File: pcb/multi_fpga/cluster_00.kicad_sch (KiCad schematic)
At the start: 7 parts, among them J1 Cluster0_SpokeBus, J2 Cluster0_Power

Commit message: Fixed C footprint.
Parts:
- C2, C3: footprint Capacitor_SMD:C_0201_0603Metric -> Capacitor_SMD:C_0603_1608Metric
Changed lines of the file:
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@@
 			)
 		)
-		(property "Footprint" "Capacitor_SMD:C_0201_0603Metric"
+		(property "Footprint" "Capacitor_SMD:C_0603_1608Metric"
 			(at 328.6252 198.12 0)
 			(hide yes)
@@
 			)
 		)
-		(property "Footprint" "Capacitor_SMD:C_0201_0603Metric"
+		(property "Footprint" "Capacitor_SMD:C_0603_1608Metric"
 			(at 290.5252 198.12 0)
 			(hide yes)
@@
 		)
 	)
+	(embedded_fonts no)
 )

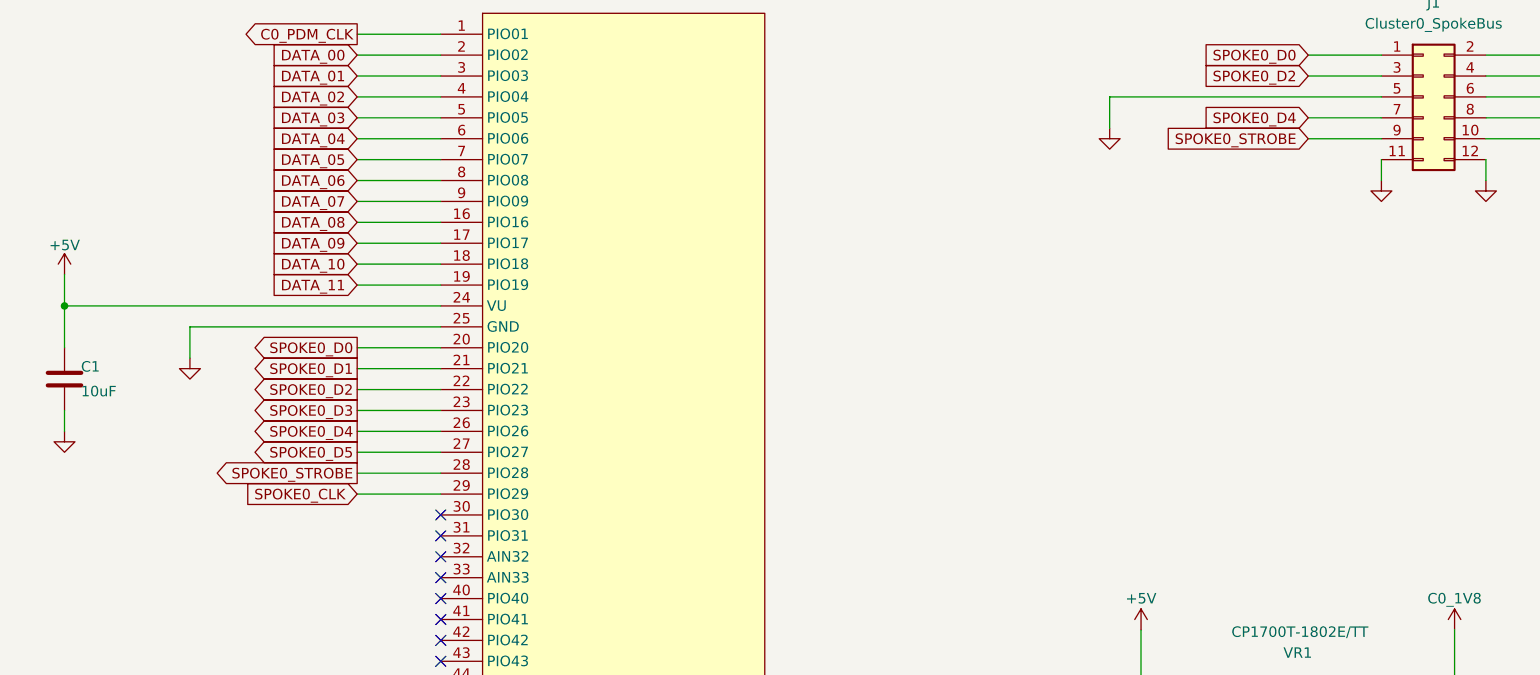
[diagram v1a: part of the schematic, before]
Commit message: Added FPGA_RESET_N signal.
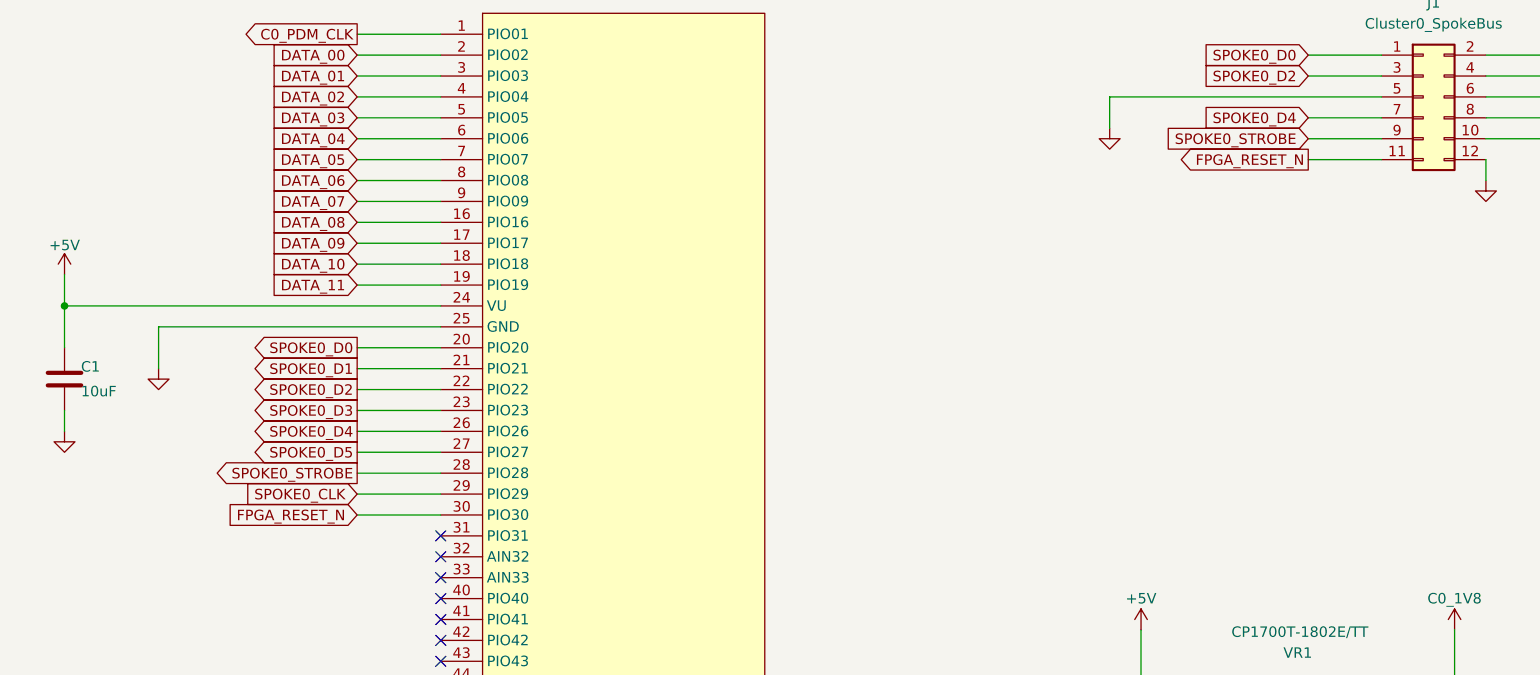
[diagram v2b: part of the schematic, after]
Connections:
- net GND: no longer J1.11 (Pin_11)
- net FPGA_RESET_N: now reaches A1.30 (PIO30)
- net FPGA_RESET_N: now also J1.11 (Pin_11)
- no-connect marks 13 -> 12
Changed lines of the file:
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@@
 	)
 	(no_connect
-		(at 204.47 167.64)
-	)
-	(no_connect
 		(at 204.47 175.26)
 	)
@@
 	(wire
 		(pts
-			(xy 173.99 144.78) (xy 204.47 144.78)
+			(xy 170.18 144.78) (xy 204.47 144.78)
 		)
 		(stroke
@@
 	(wire
 		(pts
+			(xy 204.47 167.64) (xy 194.31 167.64)
+		)
+		(stroke
+			(width 0)
+			(type default)
+		)
+	)
+	(wire
+		(pts
 			(xy 309.88 114.3) (xy 318.77 114.3)
 		)
@@
 	(wire
 		(pts
-			(xy 173.99 148.59) (xy 173.99 144.78)
+			(xy 170.18 149.86) (xy 170.18 144.78)
 		)
 		(stroke
@@
 	(wire
 		(pts
+			(xy 309.88 124.46) (xy 318.77 124.46)
+		)
+		(stroke
+			(width 0)
+			(type default)
+		)
+	)
+	(wire
+		(pts
 			(xy 331.47 111.76) (xy 342.9 111.76)
 		)
@@
 	(wire
 		(pts
-			(xy 318.77 124.46) (xy 318.77 127)
-		)
-		(stroke
-			(width 0)
-			(type default)
-		)
-	)
-	(wire
-		(pts
 			(xy 204.47 137.16) (xy 194.31 137.16)
 		)
@@
 		)
 	)
+	(global_label "FPGA_RESET_N"
+		(shape output)
+		(at 309.88 124.46 180)
+		(effects
+			(font
+				(size 1.27 1.27)
+			)
+			(justify right)
+		)
+		(property "Intersheetrefs" "${INTERSHEET_REFS}"
+			(at 309.88 124.46 180)
+			(hide yes)
+			(show_name no)
+			(do_not_autoplace no)
+			(effects
+				(font
+					(size 1.27 1.27)
+				)
+			)
+		)
+	)
 	(global_label "SPOKE0_STROBE"
 		(shape input)
@@
 		)
 	)
+	(global_label "FPGA_RESET_N"
+		(shape input)
+		(at 194.31 167.64 180)
+		(effects
+			(font
+				(size 1.27 1.27)
+			)
+			(justify right)
+		)
+		(property "Intersheetrefs" "${INTERSHEET_REFS}"
+			(at 194.31 167.64 180)
+			(hide yes)
+			(show_name no)
+			(do_not_autoplace no)
+			(effects
+				(font
+					(size 1.27 1.27)
+				)
+			)
+		)
+	)
 	(global_label "DATA_05"
 		(shape input)
@@
 	(symbol
 		(lib_id "power:GND")
-		(at 173.99 148.59 0)
+		(at 170.18 149.86 0)
 		(unit 1)
 		(body_style 1)
@@
 		(dnp no)
 		(property "Reference" "#PWR03"
-			(at 173.99 148.59 0)
+			(at 170.18 149.86 0)
 			(hide yes)
 			(show_name no)
@@
 		)
 		(property "Value" "GND"
-			(at 173.99 148.59 0)
+			(at 170.18 149.86 0)
 			(hide yes)
 			(show_name no)
@@
 		)
 		(property "Footprint" ""
-			(at 173.99 148.59 0)
+			(at 170.18 149.86 0)
 			(hide yes)
 			(show_name no)
@@
 		)
 		(property "Datasheet" ""
-			(at 173.99 148.59 0)
+			(at 170.18 149.86 0)
 			(hide yes)
 			(show_name no)
@@
 		)
 		(property "Description" "Power symbol creates a global label with name \"GND\" , ground"
-			(at 173.99 148.59 0)
+			(at 170.18 149.86 0)
 			(hide yes)
 			(show_name no)
@@
 	)
 	(symbol
-		(lib_id "power:GND")
-		(at 318.77 127 0)
-		(unit 1)
-		(body_style 1)
-		(exclude_from_sim no)
-		(in_bom yes)
-		(on_board yes)
-		(in_pos_files yes)
-		(dnp no)
-		(property "Reference" "#PWR08"
-			(at 318.77 127 0)
-			(hide yes)
-			(show_name no)
-			(do_not_autoplace no)
-			(effects
-				(font
-					(size 1.27 1.27)
-				)
-			)
-		)
-		(property "Value" "GND"
-			(at 318.77 127 0)
-			(hide yes)
-			(show_name no)
-			(do_not_autoplace no)
-			(effects
-				(font
-					(size 1.27 1.27)
-				)
-			)
-		)
-		(property "Footprint" ""
-			(at 318.77 127 0)
-			(hide yes)
-			(show_name no)
-			(do_not_autoplace no)
-			(effects
-				(font
-					(size 1.27 1.27)
-				)
-			)
-		)
-		(property "Datasheet" ""
-			(at 318.77 127 0)
-			(hide yes)
-			(show_name no)
-			(do_not_autoplace no)
-			(effects
-				(font
-					(size 1.27 1.27)
-				)
-			)
-		)
-		(property "Description" "Power symbol creates a global label with name \"GND\" , ground"
-			(at 318.77 127 0)
-			(hide yes)
-			(show_name no)
-			(do_not_autoplace no)
-			(effects
-				(font
-					(size 1.27 1.27)
-				)
-			)
-		)
-		(pin "1"
-		)
-		(instances
-			(project "top"
-				(path "/80f109c4-96c5-4385-bfb6-0f7a96b014ab/a9226103-652b-4861-8232-5e03f261e340"
-					(reference "#PWR08")
-					(unit 1)
-				)
-			)
-			(project "cluster_00"
-				(path "/b195ece8-c162-43a0-9657-a279941605a3"
-					(reference "#PWR08")
-					(unit 1)
-				)
-			)
-		)
-	)
-	(symbol
 		(lib_id "Device:C")
 		(at 158.75 151.13 0)
@@
 		)
 	)
-	(embedded_fonts no)
 )

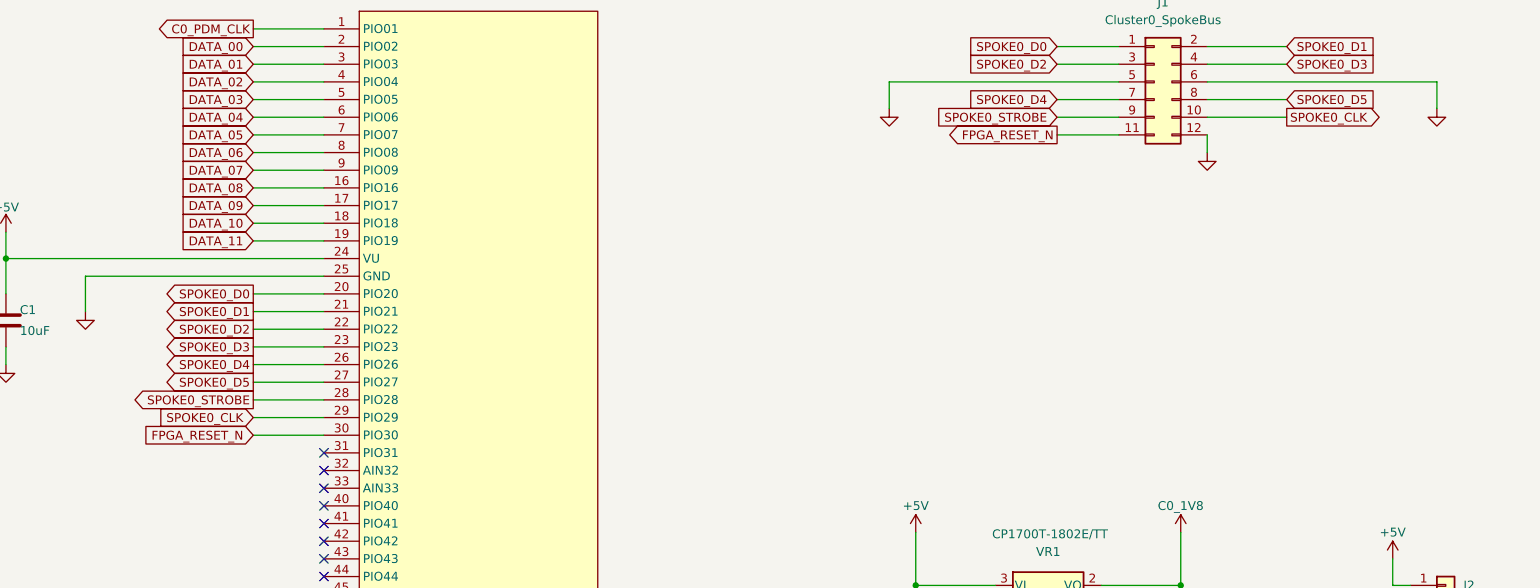
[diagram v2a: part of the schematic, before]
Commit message: Added spoke alive signals.
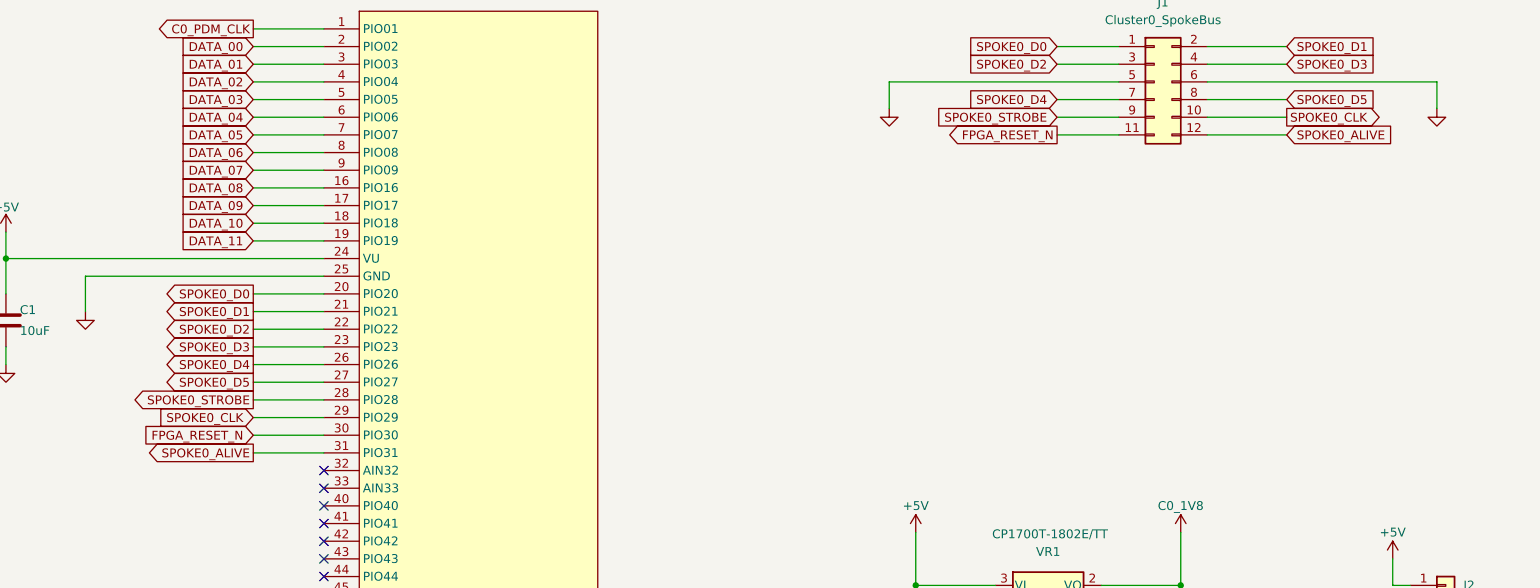
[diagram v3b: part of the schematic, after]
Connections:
- net GND: no longer J1.12 (Pin_12)
- net SPOKE0_ALIVE: now reaches A1.31 (PIO31)
- net SPOKE0_ALIVE: now also J1.12 (Pin_12)
- no-connect marks 12 -> 11
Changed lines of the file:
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@@
-	)
-	(no_connect
-		(at 204.47 170.18)
 	)
 	(no_connect
@@
 	(wire
 		(pts
+			(xy 331.47 124.46) (xy 342.9 124.46)
+		)
+		(stroke
+			(width 0)
+			(type default)
+		)
+	)
+	(wire
+		(pts
 			(xy 204.47 152.4) (xy 194.31 152.4)
 		)
@@
 	(wire
 		(pts
-			(xy 331.47 124.46) (xy 331.47 127)
-		)
-		(stroke
-			(width 0)
-			(type default)
-		)
-	)
-	(wire
-		(pts
 			(xy 327.66 181.61) (xy 327.66 189.23)
 		)
@@
 		(pts
 			(xy 327.66 189.23) (xy 316.23 189.23)
+		)
+		(stroke
+			(width 0)
+			(type default)
+		)
+	)
+	(wire
+		(pts
+			(xy 194.31 170.18) (xy 204.47 170.18)
 		)
 		(stroke
@@
 		)
 	)
+	(global_label "SPOKE0_ALIVE"
+		(shape input)
+		(at 342.9 124.46 0)
+		(fields_autoplaced yes)
+		(effects
+			(font
+				(size 1.27 1.27)
+			)
+			(justify left)
+		)
+		(property "Intersheetrefs" "${INTERSHEET_REFS}"
+			(at 359.2504 124.46 0)
+			(hide yes)
+			(show_name no)
+			(do_not_autoplace no)
+			(effects
+				(font
+					(size 1.27 1.27)
+				)
+				(justify left)
+			)
+		)
+	)
 	(global_label "FPGA_RESET_N"
 		(shape output)
@@
 					(size 1.27 1.27)
 				)
+			)
+		)
+	)
+	(global_label "SPOKE0_ALIVE"
+		(shape output)
+		(at 194.31 170.18 180)
+		(fields_autoplaced yes)
+		(effects
+			(font
+				(size 1.27 1.27)
+			)
+			(justify right)
+		)
+		(property "Intersheetrefs" "${INTERSHEET_REFS}"
+			(at 177.9596 170.18 0)
+			(hide yes)
+			(show_name no)
+			(do_not_autoplace no)
+			(effects
+				(font
+					(size 1.27 1.27)
+				)
+				(justify right)
 			)
 		)
@@
 					(unit 1)
 				)
-			)
-		)
-	)
-	(symbol
-		(lib_id "power:GND")
-		(at 331.47 127 0)
-		(unit 1)
-		(body_style 1)
-		(exclude_from_sim no)
-		(in_bom yes)
-		(on_board yes)
-		(in_pos_files yes)
-		(dnp no)
-		(property "Reference" "#PWR011"
-			(at 331.47 127 0)
-			(hide yes)
-			(show_name no)
-			(do_not_autoplace no)
-			(effects
-				(font
-					(size 1.27 1.27)
-				)
-			)
-		)
-		(property "Value" "GND"
-			(at 331.47 127 0)
-			(hide yes)
-			(show_name no)
-			(do_not_autoplace no)
-			(effects
-				(font
-					(size 1.27 1.27)
-				)
-			)
-		)
-		(property "Footprint" ""
-			(at 331.47 127 0)
-			(hide yes)
-			(show_name no)
-			(do_not_autoplace no)
-			(effects
-				(font
-					(size 1.27 1.27)
-				)
-			)
-		)
-		(property "Datasheet" ""
-			(at 331.47 127 0)
-			(hide yes)
-			(show_name no)
-			(do_not_autoplace no)
-			(effects
-				(font
-					(size 1.27 1.27)
-				)
-			)
-		)
-		(property "Description" "Power symbol creates a global label with name \"GND\" , ground"
-			(at 331.47 127 0)
-			(hide yes)
-			(show_name no)
-			(do_not_autoplace no)
-			(effects
-				(font
-					(size 1.27 1.27)
-				)
-			)
-		)
-		(pin "1"
-		)
-		(instances
-			(project "top"
-				(path "/80f109c4-96c5-4385-bfb6-0f7a96b014ab/a9226103-652b-4861-8232-5e03f261e340"
-					(reference "#PWR011")
-					(unit 1)
-				)
-			)
-			(project "cluster_00"
-				(path "/b195ece8-c162-43a0-9657-a279941605a3"
-					(reference "#PWR011")
-					(unit 1)
-				)

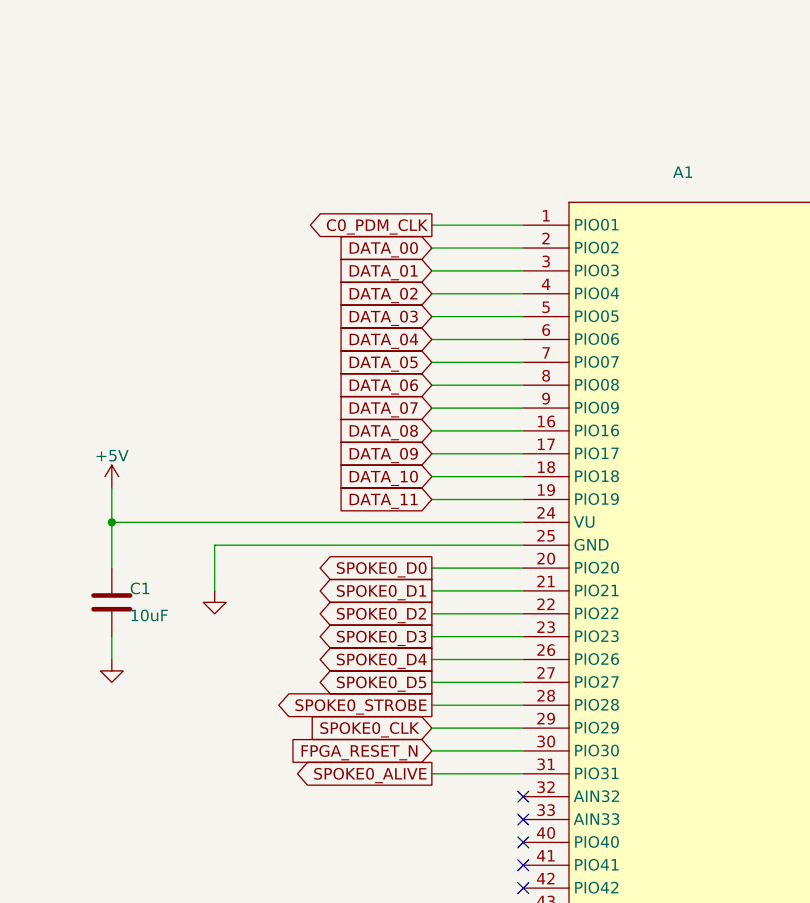
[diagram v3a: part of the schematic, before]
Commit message: Moved clock pin.
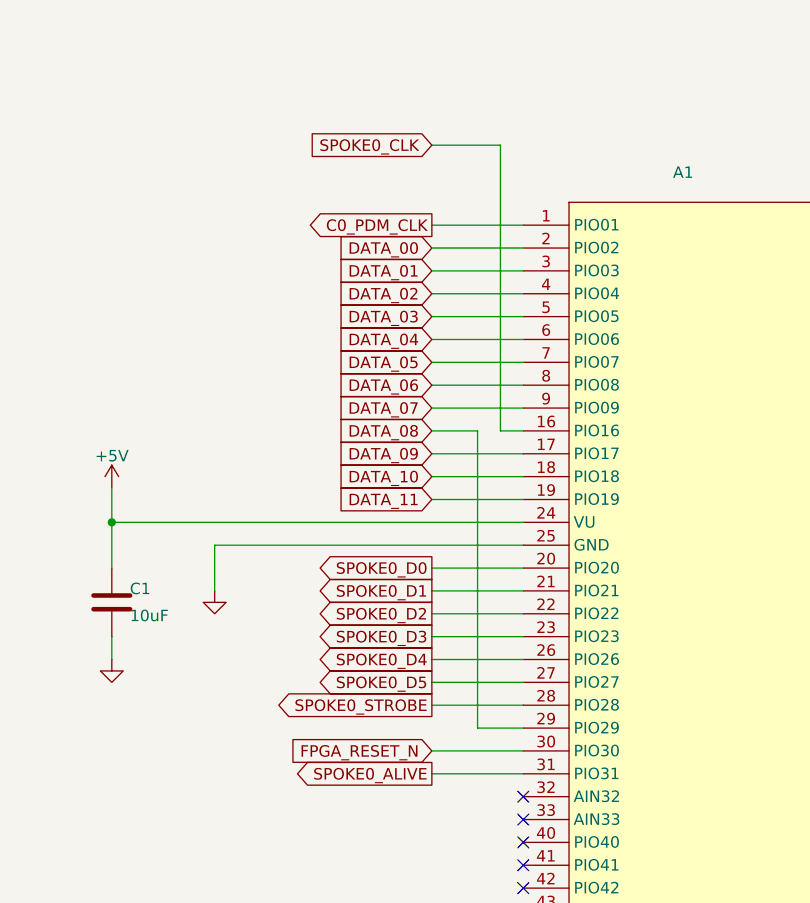
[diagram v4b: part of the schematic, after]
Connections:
- net DATA_08: now also A1.29 (PIO29); no longer A1.16 (PIO16)
- net SPOKE0_CLK: now also A1.16 (PIO16); no longer A1.29 (PIO29)
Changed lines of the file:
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@@
 	(wire
 		(pts
-			(xy 204.47 165.1) (xy 194.31 165.1)
+			(xy 204.47 165.1) (xy 199.39 165.1)
 		)
 		(stroke
@@
 	(wire
 		(pts
+			(xy 201.93 132.08) (xy 204.47 132.08)
+		)
+		(stroke
+			(width 0)
+			(type default)
+		)
+	)
+	(wire
+		(pts
 			(xy 204.47 162.56) (xy 194.31 162.56)
 		)
@@
 	(wire
 		(pts
+			(xy 194.31 132.08) (xy 199.39 132.08)
+		)
+		(stroke
+			(width 0)
+			(type default)
+		)
+	)
+	(wire
+		(pts
 			(xy 327.66 181.61) (xy 327.66 189.23)
 		)
@@
 	(wire
 		(pts
+			(xy 201.93 100.33) (xy 201.93 132.08)
+		)
+		(stroke
+			(width 0)
+			(type default)
+		)
+	)
+	(wire
+		(pts
 			(xy 358.14 185.42) (xy 358.14 189.23)
 		)
@@
 	(wire
 		(pts
+			(xy 194.31 100.33) (xy 201.93 100.33)
+		)
+		(stroke
+			(width 0)
+			(type default)
+		)
+	)
+	(wire
+		(pts
 			(xy 327.66 189.23) (xy 316.23 189.23)
 		)
@@
 	(wire
 		(pts
+			(xy 199.39 132.08) (xy 199.39 165.1)
+		)
+		(stroke
+			(width 0)
+			(type default)
+		)
+	)
+	(wire
+		(pts
 			(xy 358.14 195.58) (xy 358.14 191.77)
 		)
@@
 		(pts
 			(xy 309.88 119.38) (xy 318.77 119.38)
-		)
-		(stroke
-			(width 0)
-			(type default)
-		)
-	)
-	(wire
-		(pts
-			(xy 204.47 132.08) (xy 194.31 132.08)
 		)
 		(stroke
@@
 	(global_label "SPOKE0_CLK"
 		(shape input)
-		(at 194.31 165.1 180)
-		(effects
-			(font
-				(size 1.27 1.27)
-			)
-			(justify right)
-		)
-		(property "Intersheetrefs" "${INTERSHEET_REFS}"
-			(at 194.31 165.1 180)
-			(hide yes)
-			(show_name no)
+		(at 194.31 100.33 180)
+		(effects
+			(font
+				(size 1.27 1.27)
+			)
+			(justify right)
+		)
+		(property "Intersheetrefs" "${INTERSHEET_REFS}"
+			(at 194.31 100.33 180)
+			(hide yes)
+			(show_name no)
